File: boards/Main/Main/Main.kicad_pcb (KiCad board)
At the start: 2 copper layers, 80 x 100 mm, 33 parts, among them Q1 2N3904, Q2 2N3904, Q3 2N3904

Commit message: Add files via upload
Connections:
- Teensy4.1 pad 1: GND -> unconnected-(Teensy4.1-GND-Pad1)
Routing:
- net GND: track 217.2 -> 212.5 mm
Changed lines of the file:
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@@
 	(net 91 "unconnected-(Teensy4.1-GND-Pad64)")
 	(net 92 "unconnected-(Teensy4.1-R--Pad65)")
+	(net 93 "unconnected-(Teensy4.1-GND-Pad1)")
 	(footprint "Resistor_THT:R_Axial_DIN0309_L9.0mm_D3.2mm_P15.24mm_Horizontal"
 		(layer "F.Cu")
@@
 			(layers "*.Cu" "*.Mask")
 			(remove_unused_layers no)
-			(net 1 "GND")
+			(net 93 "unconnected-(Teensy4.1-GND-Pad1)")
 			(pinfunction "GND")
-			(pintype "power_in")
+			(pintype "power_in+no_connect")
 		)
 		(pad "2" thru_hole circle
@@
 	)
 	(segment
-		(start 101.63 73.925)
-		(end 101.85 73.705)
-		(width 0.2)
-		(layer "F.Cu")
-		(net 1)
-	)
-	(segment
-		(start 113.25 73.705)
-		(end 113 73.705)
-		(width 0.2)
-		(layer "B.Cu")
-		(net 1)
-	)
-	(segment
-		(start 114.625 68.125)
-		(end 114.625 72.33)
-		(width 0.2)
-		(layer "B.Cu")
-		(net 1)
-	)
-	(segment
 		(start 136 87.8)
 		(end 136 87.3)
@@
 	)
 	(segment
-		(start 117.399 65.351)
-		(end 114.625 68.125)
+		(start 115.89 78)
+		(end 116.99 76.9)
 		(width 0.2)
 		(layer "B.Cu")
@@
 	)
 	(segment
-		(start 113.795 73.705)
-		(end 116.99 76.9)
+		(start 101.294365 83.08)
+		(end 102.205635 83.08)
+		(width 0.2)
+		(layer "B.Cu")
+		(net 1)
+	)
+	(segment
+		(start 116.814365 85.9)
+		(end 115.89 84.975635)
 		(width 0.2)
 		(layer "B.Cu")
@@
 	)
 	(segment
-		(start 114.625 72.33)
-		(end 113.25 73.705)
+		(start 100.53 84.97)
+		(end 100.53 83.844365)
 		(width 0.2)
 		(layer "B.Cu")
@@
 	)
 	(segment
-		(start 115.89 78)
-		(end 115.89 84.975635)
-		(width 0.2)
-		(layer "B.Cu")
-		(net 1)
-	)
-	(segment
 		(start 96.75 94.92)
 		(end 96.75 106.25)
@@
 	)
 	(segment
-		(start 96.75 88.75)
-		(end 100.53 84.97)
+		(start 102.205635 83.08)
+		(end 103.5 81.785635)
+		(width 0.2)
+		(layer "B.Cu")
+		(net 1)
+	)
+	(segment
+		(start 136.599 65.351)
+		(end 117.399 65.351)
+		(width 0.2)
+		(layer "B.Cu")
+		(net 1)
+	)
+	(segment
+		(start 117.399 65.351)
+		(end 114.625 68.125)
 		(width 0.2)
 		(layer "B.Cu")
@@
 	)
 	(segment
-		(start 100.53 75.025)
-		(end 101.85 73.705)
+		(start 145.25 56.7)
+		(end 136.599 65.351)
 		(width 0.2)
 		(layer "B.Cu")
@@
 	)
 	(segment
-		(start 116.99 76.9)
-		(end 115.89 78)
+		(start 112.104365 81.785635)
+		(end 116.99 76.9)
 		(width 0.2)
 		(layer "B.Cu")
@@
 	)
 	(segment
-		(start 113 73.705)
-		(end 113.795 73.705)
+		(start 100.53 83.844365)
+		(end 101.294365 83.08)
 		(width 0.2)
 		(layer "B.Cu")
@@
 	)
 	(segment
-		(start 130.7 119.45)
-		(end 131.75 120.5)
+		(start 96.75 88.75)
+		(end 100.53 84.97)
 		(width 0.2)
 		(layer "B.Cu")
@@
 	)
 	(segment
-		(start 97.9 93.77)
-		(end 97.9 89.9)
+		(start 103.5 81.785635)
+		(end 112.104365 81.785635)
+		(width 0.2)
+		(layer "B.Cu")
+		(net 1)
+	)
+	(segment
+		(start 114.625 74.535)
+		(end 116.99 76.9)
+		(width 0.2)
+		(layer "B.Cu")
+		(net 1)
+	)
+	(segment
+		(start 130.7 119.45)
+		(end 131.75 120.5)
 		(width 0.2)
 		(layer "B.Cu")
@@
 	)
 	(segment
-		(start 101.85 73.705)
-		(end 113 73.705)
+		(start 97.9 93.77)
+		(end 97.9 89.9)
 		(width 0.2)
 		(layer "B.Cu")
@@
 	)
 	(segment
-		(start 145.25 56.7)
-		(end 136.599 65.351)
-		(width 0.2)
-		(layer "B.Cu")
-		(net 1)
-	)
-	(segment
 		(start 153.3775 130.75)
 		(end 154.5 129.6275)
@@
 	)
 	(segment
-		(start 100.53 84.97)
-		(end 100.53 75.025)
+		(start 134.6 85.9)
+		(end 135.35 86.65)
 		(width 0.2)
 		(layer "B.Cu")
@@
 	)
 	(segment
-		(start 136.599 65.351)
-		(end 117.399 65.351)
+		(start 114.625 68.125)
+		(end 114.625 74.535)
 		(width 0.2)
 		(layer "B.Cu")
@@
 	)
 	(segment
-		(start 134.6 85.9)
-		(end 135.35 86.65)
+		(start 115.89 84.975635)
+		(end 115.89 78)
 		(width 0.2)
 		(layer "B.Cu")
@@
 	)
 	(segment
-		(start 115.89 84.975635)
-		(end 116.814365 85.9)
-		(width 0.2)
-		(layer "B.Cu")
-		(net 1)
-	)
-	(segment
 		(start 116.87 73.925)
 		(end 115.77 75.025)
@@
 		(net 86)
 	)
+	(segment
+		(start 101.63 73.925)
+		(end 101.85 73.705)
+		(width 0.2)
+		(layer "F.Cu")
+		(net 93)
+	)
 	(group ""

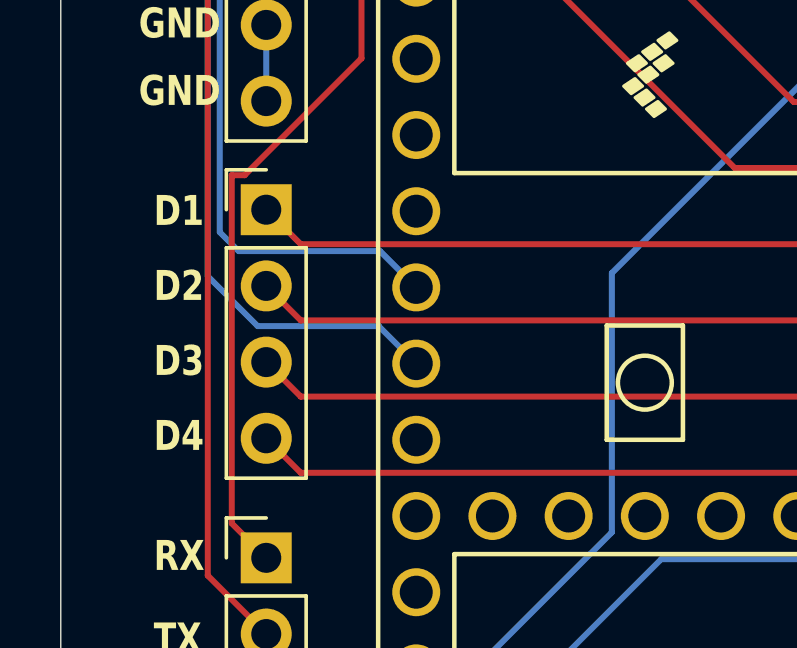
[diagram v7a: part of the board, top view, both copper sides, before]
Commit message: labelled digital input pins
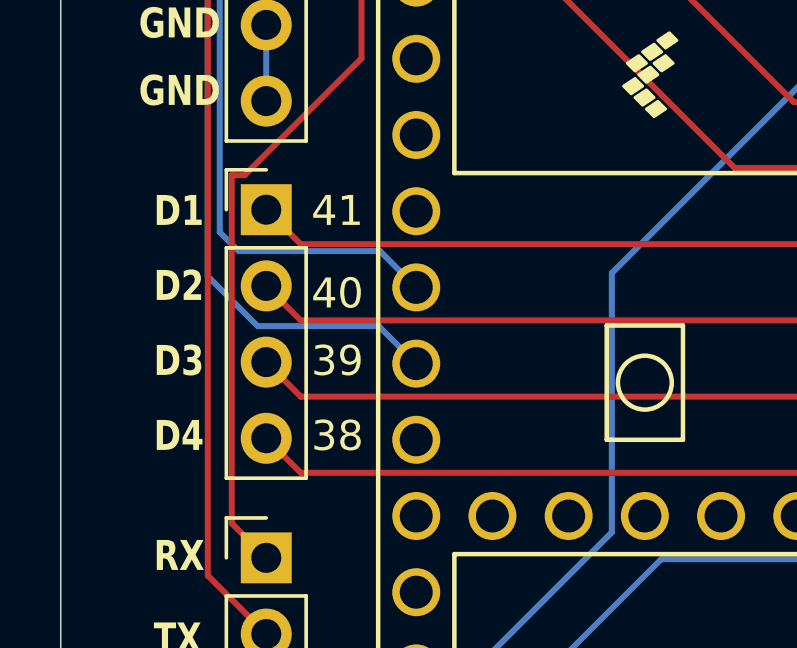
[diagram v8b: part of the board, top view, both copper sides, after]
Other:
- board text added: "38"
- board text added: "39"
- board text added: "40"
- board text added: "41"
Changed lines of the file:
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@@
+		)
+	)
+	(gr_text "39"
+		(at 98.25 115.5 0)
+		(layer "F.SilkS")
+		(effects
+			(font
+				(size 1 1)
+				(thickness 0.152)
+			)
+			(justify left bottom)
 		)
 	)
@@
 		)
 	)
+	(gr_text "41"
+		(at 98.25 110.5 0)
+		(layer "F.SilkS")
+		(effects
+			(font
+				(size 1 1)
+				(thickness 0.152)
+			)
+			(justify left bottom)
+		)
+	)
 	(gr_text "D1"
 		(at 93 110.5 0)
@@
 		)
 	)
+	(gr_text "40"
+		(at 98.25 113.25 0)
+		(layer "F.SilkS")
+		(effects
+			(font
+				(size 1 1)
+				(thickness 0.152)
+			)
+			(justify left bottom)
+		)
+	)
 	(gr_text "GND"
 		(at 92.5 101.75 0)
@@
 			)
 			(justify left bottom)
+		)
+	)
+	(gr_text "38"
+		(at 98.25 118 0)
+		(layer "F.SilkS")
+		(effects
+			(font
+				(size 1 1)
+				(thickness 0.152)
+			)
+			(justify left bottom)
